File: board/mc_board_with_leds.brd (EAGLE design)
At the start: 131 x 76.6 mm, 30 parts, among them IC2 MEGA8-P, Q2 16MHz

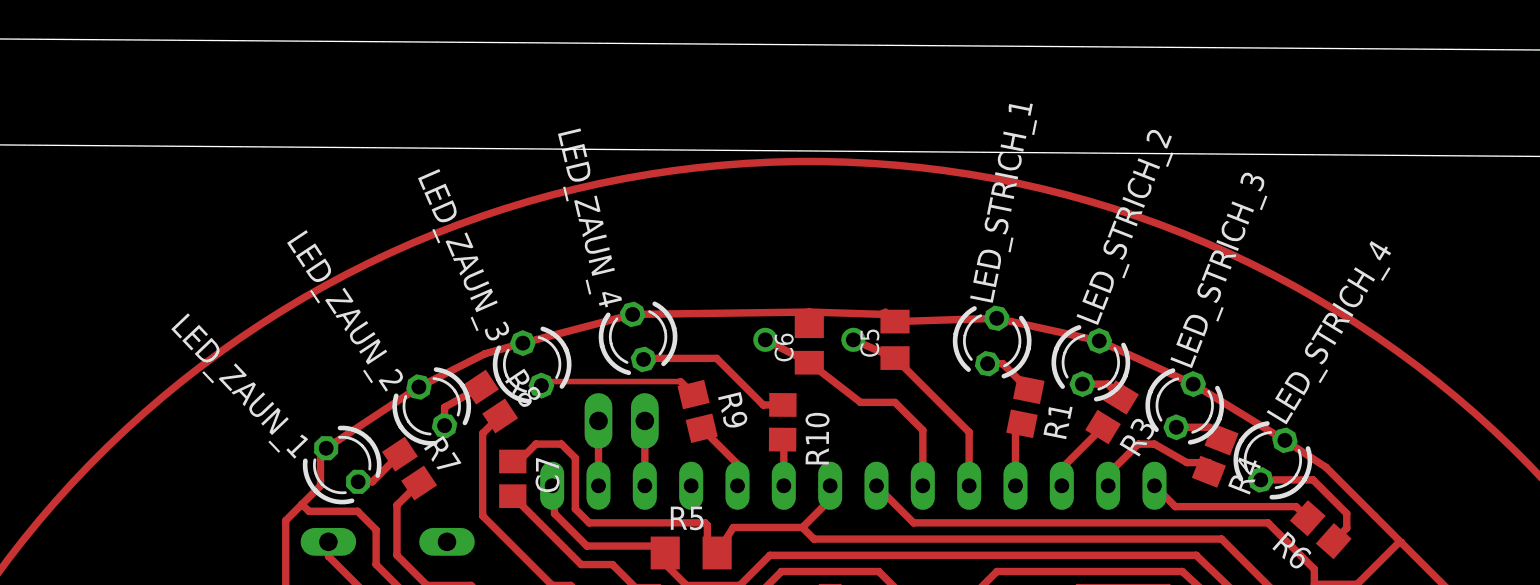
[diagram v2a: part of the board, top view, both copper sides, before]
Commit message: reordered leds
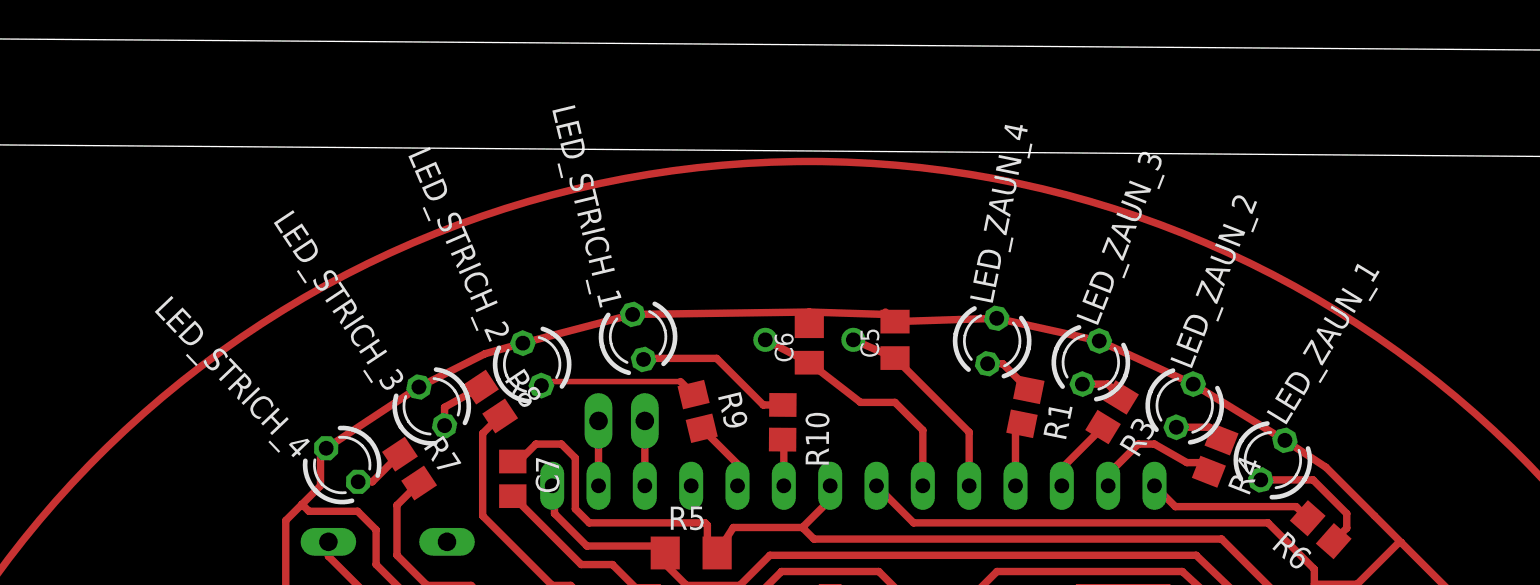
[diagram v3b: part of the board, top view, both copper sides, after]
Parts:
- moved LED_STRICH_4 51.0 mm to (29.6, 38.5), turned to 133.6 degrees
- moved LED_ZAUN_1 51.0 mm to (80.7, 38.7), turned to 58.6 degrees
- moved LED_STRICH_3 41.3 mm to (34.5, 41.7), turned to 123.6 degrees
- moved LED_ZAUN_2 41.3 mm to (75.8, 41.7), turned to 68.6 degrees
- moved LED_STRICH_2 30.6 mm to (40.0, 44.0), turned to 113.6 degrees
- moved LED_ZAUN_3 30.6 mm to (70.7, 44.1), turned to 68.6 degrees
- moved LED_STRICH_1 19.4 mm to (45.9, 45.5), turned to 103.6 degrees
- moved LED_ZAUN_4 19.4 mm to (65.3, 45.3), turned to 78.6 degrees
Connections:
- net PB0/LED_STRICH_4 renamed PB0/LED_ZAUN_1
- net PC4/LED_ZAUN_2 renamed PC4/LED_STRICH_3
- net PC5/LED_ZAUN_1 renamed PC5/LED_STRICH_4
- net PD3/LED_ZAUN_3 renamed PD3/LED_STRICH_2
- net PD4/LED_ZAUN_4 renamed PD4/LED_STRICH_1
- net PD5/LED_STRICH_1 renamed PD5/LED_ZAUN_4
- net PD6/LED_STRICH_2 renamed PD6/LED_ZAUN_3
- net PD7/LED_STRICH_3 renamed PD7/LED_ZAUN_2
- net N$1: now also LED_ZAUN_4.A; no longer LED_STRICH_1.A
- net N$10: now also LED_STRICH_3.A; no longer LED_ZAUN_2.A
- net N$11: now also LED_STRICH_2.A; no longer LED_ZAUN_3.A
- net N$12: now also LED_STRICH_1.A; no longer LED_ZAUN_4.A
- net N$2: now also LED_ZAUN_3.A; no longer LED_STRICH_2.A
- net N$3: now also LED_ZAUN_2.A; no longer LED_STRICH_3.A
- net N$7: now also LED_ZAUN_1.A; no longer LED_STRICH_4.A
- net N$8: now also LED_STRICH_4.A; no longer LED_ZAUN_1.A
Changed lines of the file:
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@@
 </autorouter>
 <elements>
-<element name="LED_STRICH_1" library="led" package="LED3MM" value="" x="65.26883125" y="45.27481875" rot="R78.6"/>
-<element name="LED_STRICH_2" library="led" package="LED3MM" value="" x="70.6780875" y="44.09545625" rot="R68.6"/>
-<element name="LED_STRICH_3" library="led" package="LED3MM" value="" x="75.826471875" y="41.72945625" rot="R68.6"/>
-<element name="LED_STRICH_4" library="led" package="LED3MM" value="" x="80.6571" y="38.7449125" rot="R58.6"/>
-<element name="LED_ZAUN_1" library="led" package="LED3MM" value="" x="29.6350125" y="38.4763" rot="R133.6"/>
-<element name="LED_ZAUN_2" library="led" package="LED3MM" value="" x="34.5460125" y="41.69431875" rot="R123.6"/>
-<element name="LED_ZAUN_3" library="led" package="LED3MM" value="" x="40.04930625" y="43.994065625" rot="R113.6"/>
-<element name="LED_ZAUN_4" library="led" package="LED3MM" value="" x="45.85698125" y="45.498234375" rot="R103.6"/>
+<element name="LED_ZAUN_4" library="led" package="LED3MM" value="" x="65.26883125" y="45.27481875" rot="R78.6"/>
+<element name="LED_ZAUN_3" library="led" package="LED3MM" value="" x="70.6780875" y="44.09545625" rot="R68.6"/>
+<element name="LED_ZAUN_2" library="led" package="LED3MM" value="" x="75.826471875" y="41.72945625" rot="R68.6"/>
+<element name="LED_ZAUN_1" library="led" package="LED3MM" value="" x="80.6571" y="38.7449125" rot="R58.6"/>
+<element name="LED_STRICH_4" library="led" package="LED3MM" value="" x="29.6350125" y="38.4763" rot="R133.6"/>
+<element name="LED_STRICH_3" library="led" package="LED3MM" value="" x="34.5460125" y="41.69431875" rot="R123.6"/>
+<element name="LED_STRICH_2" library="led" package="LED3MM" value="" x="40.04930625" y="43.994065625" rot="R113.6"/>
+<element name="LED_STRICH_1" library="led" package="LED3MM" value="" x="45.85698125" y="45.498234375" rot="R103.6"/>
 <element name="R1" library="resistor" package="R0805" value="470" x="67.091109375" y="41.668040625" rot="R258.6"/>
 <element name="R3" library="resistor" package="R0805" value="470" x="71.842928125" y="41.36911875" rot="R238.6"/>
@@
 </signal>
 <signal name="GND">
+<contactref element="LED_ZAUN_4" pad="K"/>
+<contactref element="LED_ZAUN_3" pad="K"/>
+<contactref element="LED_ZAUN_2" pad="K"/>
+<contactref element="LED_ZAUN_1" pad="K"/>
+<contactref element="LED_STRICH_4" pad="K"/>
+<contactref element="LED_STRICH_3" pad="K"/>
+<contactref element="LED_STRICH_2" pad="K"/>
 <contactref element="LED_STRICH_1" pad="K"/>
-<contactref element="LED_STRICH_2" pad="K"/>
-<contactref element="LED_STRICH_3" pad="K"/>
-<contactref element="LED_STRICH_4" pad="K"/>
-<contactref element="LED_ZAUN_1" pad="K"/>
-<contactref element="LED_ZAUN_2" pad="K"/>
-<contactref element="LED_ZAUN_3" pad="K"/>
-<contactref element="LED_ZAUN_4" pad="K"/>
 <contactref element="PWRLED" pad="K"/>
 <contactref element="IC2" pad="8"/>
@@
 <contactref element="IC2" pad="16"/>
 </signal>
-<signal name="PD3/LED_ZAUN_3">
+<signal name="PD3/LED_STRICH_2">
 <contactref element="IC2" pad="5"/>
 <contactref element="R9" pad="2"/>
@@
 <wire x1="51.308" y1="38.52985" x2="49.34691875" y2="40.49093125" width="0.4064" layer="1"/>
 </signal>
-<signal name="PD4/LED_ZAUN_4">
+<signal name="PD4/LED_STRICH_1">
 <contactref element="IC2" pad="6"/>
 <contactref element="R10" pad="2"/>
@@
 <wire x1="46.228" y1="37.338" x2="46.228" y2="40.894" width="0.4064" layer="1"/>
 </signal>
-<signal name="PC5/LED_ZAUN_1">
+<signal name="PC5/LED_STRICH_4">
 <contactref element="IC2" pad="28"/>
 <contactref element="R7" pad="2"/>
@@
 <wire x1="32.639" y1="36.27205625" x2="33.855384375" y2="37.488440625" width="0.4064" layer="1"/>
 </signal>
-<signal name="PC4/LED_ZAUN_2">
+<signal name="PC4/LED_STRICH_3">
 <contactref element="IC2" pad="27"/>
 <contactref element="R8" pad="2"/>
@@
 <signal name="N$1">
 <contactref element="R1" pad="1"/>
-<contactref element="LED_STRICH_1" pad="A"/>
+<contactref element="LED_ZAUN_4" pad="A"/>
 <wire x1="67.27888125" y1="42.599296875" x2="65.84830625" y2="44.029871875" width="0.4064" layer="1"/>
 <wire x1="65.84830625" y1="44.029871875" x2="65.01780625" y2="44.029871875" width="0.4064" layer="1"/>
@@
 <signal name="N$2">
 <contactref element="R3" pad="1"/>
-<contactref element="LED_STRICH_2" pad="A"/>
+<contactref element="LED_ZAUN_3" pad="A"/>
 <wire x1="72.337884375" y1="42.179990625" x2="71.6048625" y2="42.9130125" width="0.4064" layer="1"/>
 <wire x1="71.6048625" y1="42.9130125" x2="70.21469375" y2="42.9130125" width="0.4064" layer="1"/>
@@
 <signal name="N$3">
 <contactref element="R4" pad="1"/>
-<contactref element="LED_STRICH_3" pad="A"/>
+<contactref element="LED_ZAUN_2" pad="A"/>
 <wire x1="77.842928125" y1="39.87685" x2="77.172765625" y2="40.5470125" width="0.4064" layer="1"/>
 <wire x1="77.172765625" y1="40.5470125" x2="75.363078125" y2="40.5470125" width="0.4064" layer="1"/>
@@
 <signal name="N$7">
 <contactref element="R6" pad="1"/>
-<contactref element="LED_STRICH_4" pad="A"/>
+<contactref element="LED_ZAUN_1" pad="A"/>
 <wire x1="83.99415625" y1="34.30281875" x2="84.709" y2="35.0176625" width="0.4064" layer="1"/>
 <wire x1="84.709" y1="35.0176625" x2="84.709" y2="35.814" width="0.4064" layer="1"/>
@@
 <signal name="N$8">
 <contactref element="R7" pad="1"/>
-<contactref element="LED_ZAUN_1" pad="A"/>
+<contactref element="LED_STRICH_4" pad="A"/>
 <wire x1="30.510828125" y1="37.5566" x2="31.28954375" y2="37.5566" width="0.4064" layer="1"/>
 <wire x1="31.28954375" y1="37.5566" x2="32.8039375" y2="39.07099375" width="0.4064" layer="1"/>
@@
 <signal name="N$10">
 <contactref element="R8" pad="1"/>
-<contactref element="LED_ZAUN_2" pad="A"/>
+<contactref element="LED_STRICH_3" pad="A"/>
 <wire x1="37.2447625" y1="42.748709375" x2="35.24881875" y2="41.641765625" width="0.4064" layer="1"/>
 <wire x1="35.24881875" y1="41.641765625" x2="35.24881875" y2="40.63650625" width="0.4064" layer="1"/>
@@
 <signal name="N$11">
 <contactref element="R9" pad="1"/>
-<contactref element="LED_ZAUN_3" pad="A"/>
+<contactref element="LED_STRICH_2" pad="A"/>
 <wire x1="48.900146875" y1="42.337659375" x2="48.18480625" y2="43.053" width="0.4064" layer="1"/>
 <wire x1="48.18480625" y1="43.053" x2="40.7804625" y2="43.053" width="0.3048" layer="1"/>
@@
 <signal name="N$12">
 <contactref element="R10" pad="1"/>
-<contactref element="LED_ZAUN_4" pad="A"/>
+<contactref element="LED_STRICH_1" pad="A"/>
 <wire x1="53.795171875" y1="41.769384375" x2="52.718615625" y2="41.769384375" width="0.4064" layer="1"/>
 <wire x1="52.718615625" y1="41.769384375" x2="50.165" y2="44.323" width="0.4064" layer="1"/>
@@
 <wire x1="42.738" y1="33.02" x2="38.989" y2="36.769" width="0.4064" layer="1"/>
 </signal>
-<signal name="PB0/LED_STRICH_4">
+<signal name="PB0/LED_ZAUN_1">
 <contactref element="IC2" pad="14"/>
 <contactref element="R6" pad="2"/>
@@
 <contactref element="IC2" pad="15"/>
 </signal>
-<signal name="PD5/LED_STRICH_1">
+<signal name="PD5/LED_ZAUN_4">
 <contactref element="R1" pad="2"/>
 <contactref element="IC2" pad="11"/>
@@
 <wire x1="66.903334375" y1="40.381446875" x2="66.903334375" y2="40.73678125" width="0.4064" layer="1"/>
 </signal>
-<signal name="PD6/LED_STRICH_2">
+<signal name="PD6/LED_ZAUN_3">
 <contactref element="R3" pad="2"/>
 <contactref element="IC2" pad="12"/>
@@
 <wire x1="69.088" y1="38.298275" x2="71.34796875" y2="40.55824375" width="0.4064" layer="1"/>
 </signal>
-<signal name="PD7/LED_STRICH_3">
+<signal name="PD7/LED_ZAUN_2">
 <contactref element="R4" pad="2"/>
 <contactref element="IC2" pad="13"/>
@@
 <wire x1="73.279" y1="39.624" x2="71.628" y2="37.973" width="0.4064" layer="1"/>
 <wire x1="71.628" y1="37.973" x2="71.628" y2="37.338" width="0.4064" layer="1"/>
-<wire x1="75.946" y1="38.608" x2="77.1496625" y2="38.608" width="0.4064" layer="1"/>
-<wire x1="77.1496625" y1="38.608" x2="77.1496625" y2="38.107846875" width="0.4064" layer="1"/>
+<wire x1="75.946" y1="38.608" x2="76.649509375" y2="38.608" width="0.4064" layer="1"/>
+<wire x1="76.649509375" y1="38.608" x2="77.1496625" y2="38.107846875" width="0.4064" layer="1"/>
 </signal>
 </signals>

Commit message: small changes
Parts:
- moved LED_STRICH_4 0.57 mm to (30.1, 38.7)
- moved R7 0.51 mm to (33.8, 38.3)
- moved R8 0.51 mm to (38.3, 42.0)
- moved LED_STRICH_3 0.40 mm to (34.9, 41.8)
- moved LED_STRICH_2 0.28 mm to (40.3, 44.1)
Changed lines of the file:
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@@
 <element name="LED_ZAUN_2" library="led" package="LED3MM" value="" x="75.826471875" y="41.72945625" rot="R68.6"/>
 <element name="LED_ZAUN_1" library="led" package="LED3MM" value="" x="80.6571" y="38.7449125" rot="R58.6"/>
-<element name="LED_STRICH_4" library="led" package="LED3MM" value="" x="29.6350125" y="38.4763" rot="R133.6"/>
-<element name="LED_STRICH_3" library="led" package="LED3MM" value="" x="34.5460125" y="41.69431875" rot="R123.6"/>
-<element name="LED_STRICH_2" library="led" package="LED3MM" value="" x="40.04930625" y="43.994065625" rot="R113.6"/>
+<element name="LED_STRICH_4" library="led" package="LED3MM" value="" x="30.1430125" y="38.7303" rot="R133.6"/>
+<element name="LED_STRICH_3" library="led" package="LED3MM" value="" x="34.9270125" y="41.82131875" rot="R123.6"/>
+<element name="LED_STRICH_2" library="led" package="LED3MM" value="" x="40.30330625" y="44.121065625" rot="R113.6"/>
 <element name="LED_STRICH_1" library="led" package="LED3MM" value="" x="45.85698125" y="45.498234375" rot="R103.6"/>
 <element name="R1" library="resistor" package="R0805" value="470" x="67.091109375" y="41.668040625" rot="R258.6"/>
@@
 <element name="R4" library="resistor" package="R0805" value="470" x="77.496296875" y="38.99235" rot="R248.6"/>
 <element name="R6" library="resistor" package="R0805" value="470" x="83.281553125" y="34.931065625" rot="R138.6"/>
-<element name="R7" library="resistor" package="R0805" value="470" x="33.3296625" y="38.27971875" rot="R303.6"/>
-<element name="R8" library="resistor" package="R0805" value="470" x="37.7704875" y="41.957434375" rot="R303.6"/>
+<element name="R7" library="resistor" package="R0805" value="470" x="33.8376625" y="38.27971875" rot="R303.6"/>
+<element name="R8" library="resistor" package="R0805" value="470" x="38.2784875" y="41.957434375" rot="R303.6"/>
 <element name="R9" library="resistor" package="R0805" value="470" x="49.123534375" y="41.414296875" rot="R283.6"/>
 <element name="R10" library="resistor" package="R0805" value="470" x="53.788540625" y="40.819409375" rot="R269.6"/>
@@
 <wire x1="27.432" y1="36.322" x2="28.448" y2="37.338" width="0.4064" layer="1"/>
 <wire x1="28.448" y1="37.338" x2="28.448" y2="39.084803125" width="0.4064" layer="1"/>
-<wire x1="28.448" y1="39.084803125" x2="28.75919375" y2="39.395996875" width="0.4064" layer="1"/>
+<wire x1="28.448" y1="39.084803125" x2="29.26719375" y2="39.649996875" width="0.4064" layer="1"/>
 <wire x1="35.3822" y1="29.7434" x2="34.7726" y2="29.7434" width="0.4064" layer="1"/>
 <wire x1="34.7726" y1="29.7434" x2="31.496" y2="33.02" width="0.4064" layer="1"/>
@@
 <wire x1="59.555" y1="46.728" x2="59.42" y2="46.863" width="0.4064" layer="1"/>
 <wire x1="55.245" y1="46.863" x2="55.245" y2="46.085" width="0.4064" layer="1"/>
-<wire x1="45.55835" y1="46.732621875" x2="39.5408625" y2="45.15784375" width="0.4064" layer="1"/>
-<wire x1="39.5408625" y1="45.15784375" x2="37.465" y2="44.577" width="0.4064" layer="1"/>
-<wire x1="37.465" y1="44.577" x2="33.843203125" y2="42.752128125" width="0.4064" layer="1"/>
-<wire x1="33.843203125" y1="42.752128125" x2="28.75919375" y2="39.395996875" width="0.4064" layer="1"/>
+<wire x1="45.55835" y1="46.732621875" x2="39.7948625" y2="45.28484375" width="0.4064" layer="1"/>
+<wire x1="39.7948625" y1="45.28484375" x2="37.465" y2="44.577" width="0.4064" layer="1"/>
+<wire x1="37.465" y1="44.577" x2="34.224203125" y2="42.879128125" width="0.4064" layer="1"/>
+<wire x1="34.224203125" y1="42.879128125" x2="29.26719375" y2="39.649996875" width="0.4064" layer="1"/>
 <wire x1="55.245" y1="46.863" x2="45.55835" y2="46.732621875" width="0.4064" layer="1"/>
 <wire x1="55.245" y1="46.863" x2="59.555" y2="46.728" width="0.4064" layer="1"/>
@@
 <wire x1="34.29" y1="31.877" x2="32.639" y2="33.528" width="0.4064" layer="1"/>
 <wire x1="32.639" y1="33.528" x2="32.639" y2="36.27205625" width="0.4064" layer="1"/>
-<wire x1="32.639" y1="36.27205625" x2="33.855384375" y2="37.488440625" width="0.4064" layer="1"/>
+<wire x1="32.639" y1="36.27205625" x2="34.363384375" y2="37.488440625" width="0.4064" layer="1"/>
 </signal>
 <signal name="PC4/LED_STRICH_3">
@@
 <wire x1="41.148" y1="31.877" x2="37.338" y2="35.687" width="0.4064" layer="1"/>
 <wire x1="37.338" y1="35.687" x2="37.338" y2="40.207946875" width="0.4064" layer="1"/>
-<wire x1="37.338" y1="40.207946875" x2="38.296209375" y2="41.16615625" width="0.4064" layer="1"/>
+<wire x1="37.338" y1="40.207946875" x2="38.804209375" y2="41.16615625" width="0.4064" layer="1"/>
 </signal>
 <signal name="N$1">
@@
 <contactref element="R7" pad="1"/>
 <contactref element="LED_STRICH_4" pad="A"/>
-<wire x1="30.510828125" y1="37.5566" x2="31.28954375" y2="37.5566" width="0.4064" layer="1"/>
-<wire x1="31.28954375" y1="37.5566" x2="32.8039375" y2="39.07099375" width="0.4064" layer="1"/>
+<wire x1="31.018828125" y1="37.8106" x2="31.28954375" y2="37.5566" width="0.4064" layer="1"/>
+<wire x1="31.28954375" y1="37.5566" x2="33.3119375" y2="39.07099375" width="0.4064" layer="1"/>
 </signal>
 <signal name="N$10">
 <contactref element="R8" pad="1"/>
 <contactref element="LED_STRICH_3" pad="A"/>
-<wire x1="37.2447625" y1="42.748709375" x2="35.24881875" y2="41.641765625" width="0.4064" layer="1"/>
-<wire x1="35.24881875" y1="41.641765625" x2="35.24881875" y2="40.63650625" width="0.4064" layer="1"/>
+<wire x1="37.7527625" y1="42.748709375" x2="35.24881875" y2="41.641765625" width="0.4064" layer="1"/>
+<wire x1="35.24881875" y1="41.641765625" x2="35.62981875" y2="40.76350625" width="0.4064" layer="1"/>
 </signal>
 <signal name="N$11">
@@
 <wire x1="48.900146875" y1="42.337659375" x2="48.18480625" y2="43.053" width="0.4064" layer="1"/>
 <wire x1="48.18480625" y1="43.053" x2="40.7804625" y2="43.053" width="0.3048" layer="1"/>
-<wire x1="40.557746875" y1="42.830284375" x2="40.7804625" y2="43.053" width="0.4064" layer="1"/>
+<wire x1="40.811746875" y1="42.957284375" x2="40.7804625" y2="43.053" width="0.4064" layer="1"/>
 </signal>
 <signal name="N$12">
